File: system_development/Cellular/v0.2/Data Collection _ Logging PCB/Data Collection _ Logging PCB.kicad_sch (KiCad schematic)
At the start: 8 parts, among them U1 TC2014-3.3VxCTTR

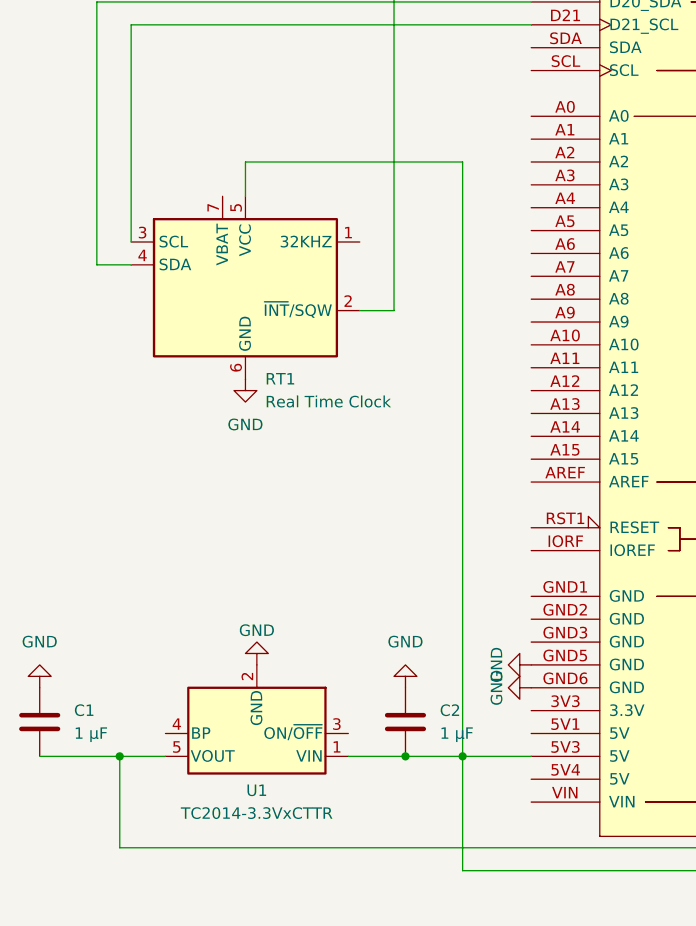
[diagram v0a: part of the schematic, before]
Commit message: Updated PCB Files
Updated Datalogging PCB to correct sizing mistakes
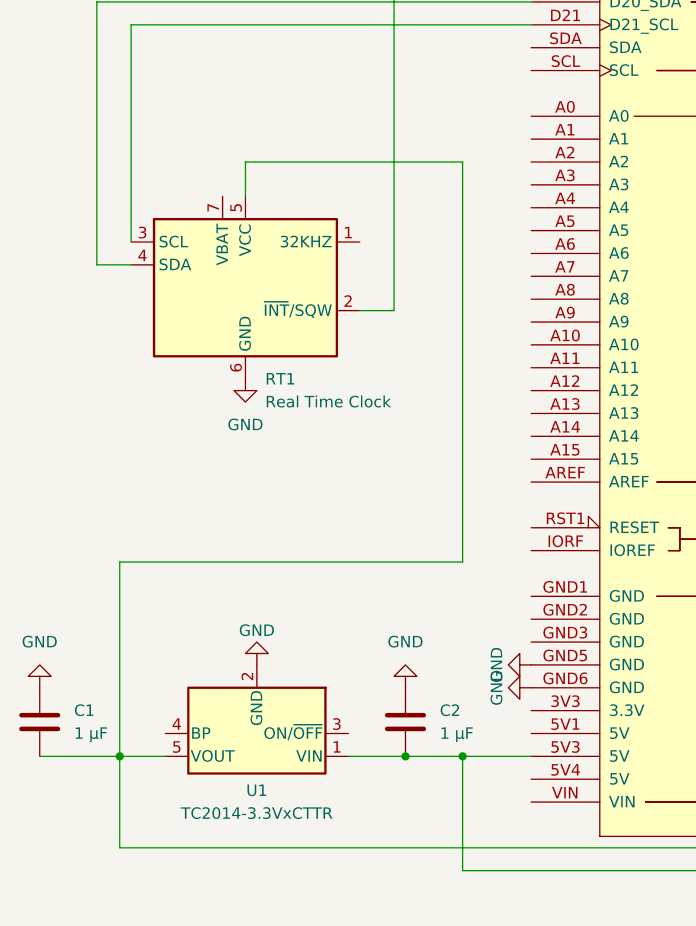
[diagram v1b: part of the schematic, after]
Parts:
- Micro_SD1, RT1: footprint Connector_PinSocket_1.00mm:PinSocket_1x06_P1.00mm_Vertical -> Connector_PinSocket_2.54mm:PinSocket_1x06_P2.54mm_Vertical
- US1, US2: footprint Connector_PinSocket_1.00mm:PinSocket_1x04_P1.00mm_Vertical -> Connector_PinSocket_2.54mm:PinSocket_1x04_P2.54mm_Vertical
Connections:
- net at C1.2, Micro_SD1.1 (3.3V), U1.5 (VOUT): now also RT1.5 (VCC)
- net at C2.2, U1.1 (VIN), US1.4 (VCC)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: no longer RT1.5 (VCC)
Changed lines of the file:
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@@
   (junction (at 90.17 144.78) (diameter 0) (color 0 0 0 0)
   )
+  (wire (pts (xy 58.42 123.19) (xy 58.42 144.78))
+    (stroke (width 0) (type default))
+  )
   (wire (pts (xy 203.2 99.06) (xy 203.2 132.08))
     (stroke (width 0) (type default))
@@
     (stroke (width 0) (type default))
   )
-  (wire (pts (xy 96.52 78.74) (xy 96.52 144.78))
-    (stroke (width 0) (type default))
-  )
   (wire (pts (xy 199.39 142.24) (xy 218.44 142.24))
     (stroke (width 0) (type default))
@@
     (stroke (width 0) (type default))
   )
-  (wire (pts (xy 58.42 154.94) (xy 58.42 144.78))
-    (stroke (width 0) (type default))
-  )
   (wire (pts (xy 227.33 87.63) (xy 208.28 87.63))
     (stroke (width 0) (type default))
   )
+  (wire (pts (xy 96.52 123.19) (xy 58.42 123.19))
+    (stroke (width 0) (type default))
+  )
   (wire (pts (xy 96.52 144.78) (xy 96.52 157.48))
     (stroke (width 0) (type default))
   )
+  (wire (pts (xy 96.52 78.74) (xy 96.52 123.19))
+    (stroke (width 0) (type default))
+  )
   (wire (pts (xy 210.82 139.7) (xy 218.44 139.7))
     (stroke (width 0) (type default))
@@
   )
   (wire (pts (xy 96.52 157.48) (xy 208.28 157.48))
+    (stroke (width 0) (type default))
+  )
+  (wire (pts (xy 58.42 144.78) (xy 58.42 154.94))
     (stroke (width 0) (type default))
   )
@@
       (effects (font (size 1.27 1.27)) (justify left))
     )
-    (property "Footprint" "Connector_PinSocket_1.00mm:PinSocket_1x04_P1.00mm_Vertical" (at 234.95 101.6 0)
+    (property "Footprint" "Connector_PinSocket_2.54mm:PinSocket_1x04_P2.54mm_Vertical" (at 234.95 101.6 0)
       (effects (font (size 1.27 1.27)) hide)
     )
@@
       (effects (font (size 1.27 1.27)) (justify left))
     )
-    (property "Footprint" "Connector_PinSocket_1.00mm:PinSocket_1x04_P1.00mm_Vertical" (at 234.95 82.55 0)
+    (property "Footprint" "Connector_PinSocket_2.54mm:PinSocket_1x04_P2.54mm_Vertical" (at 234.95 82.55 0)
       (effects (font (size 1.27 1.27)) hide)
     )
@@
       (effects (font (size 1.27 1.27)) (justify left))
     )
-    (property "Footprint" "Connector_PinSocket_1.00mm:PinSocket_1x06_P1.00mm_Vertical" (at 238.76 143.51 0)
+    (property "Footprint" "Connector_PinSocket_2.54mm:PinSocket_1x06_P2.54mm_Vertical" (at 238.76 143.51 0)
       (effects (font (size 1.27 1.27)) hide)
     )
@@
       (effects (font (size 1.27 1.27)) (justify left))
     )
-    (property "Footprint" "Connector_PinSocket_1.00mm:PinSocket_1x06_P1.00mm_Vertical" (at 73.66 105.41 0)
-      (effects (font (size 1.27 1.27)) hide)
-    )
+    (property "Footprint" "Connector_PinSocket_2.54mm:PinSocket_1x06_P2.54mm_Vertical" (at 73.66 105.41 0)
+      (effects (font (size 1.27 1.27)) hide)
+    )
